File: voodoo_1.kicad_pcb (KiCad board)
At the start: 2 copper layers, 1 part, among them U1 LM301

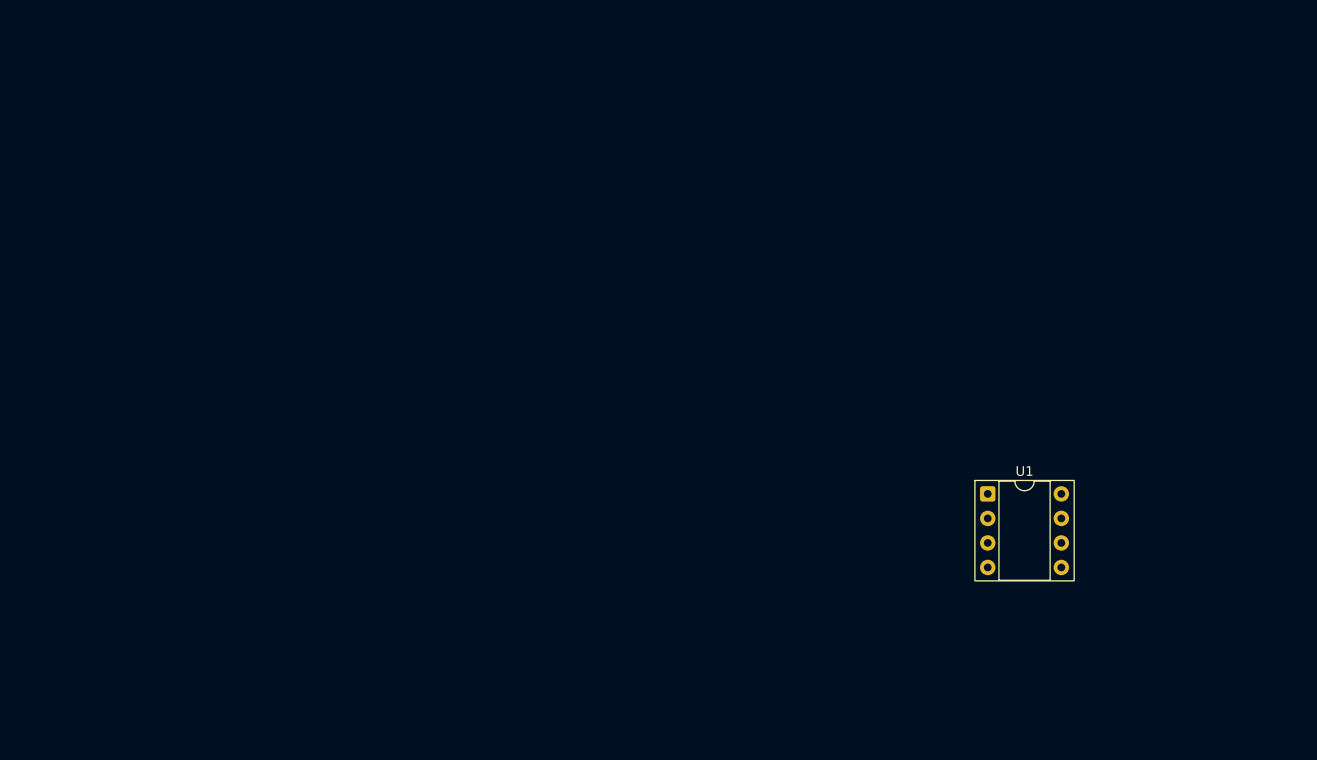
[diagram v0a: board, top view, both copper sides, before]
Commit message: フットプリント割り当て
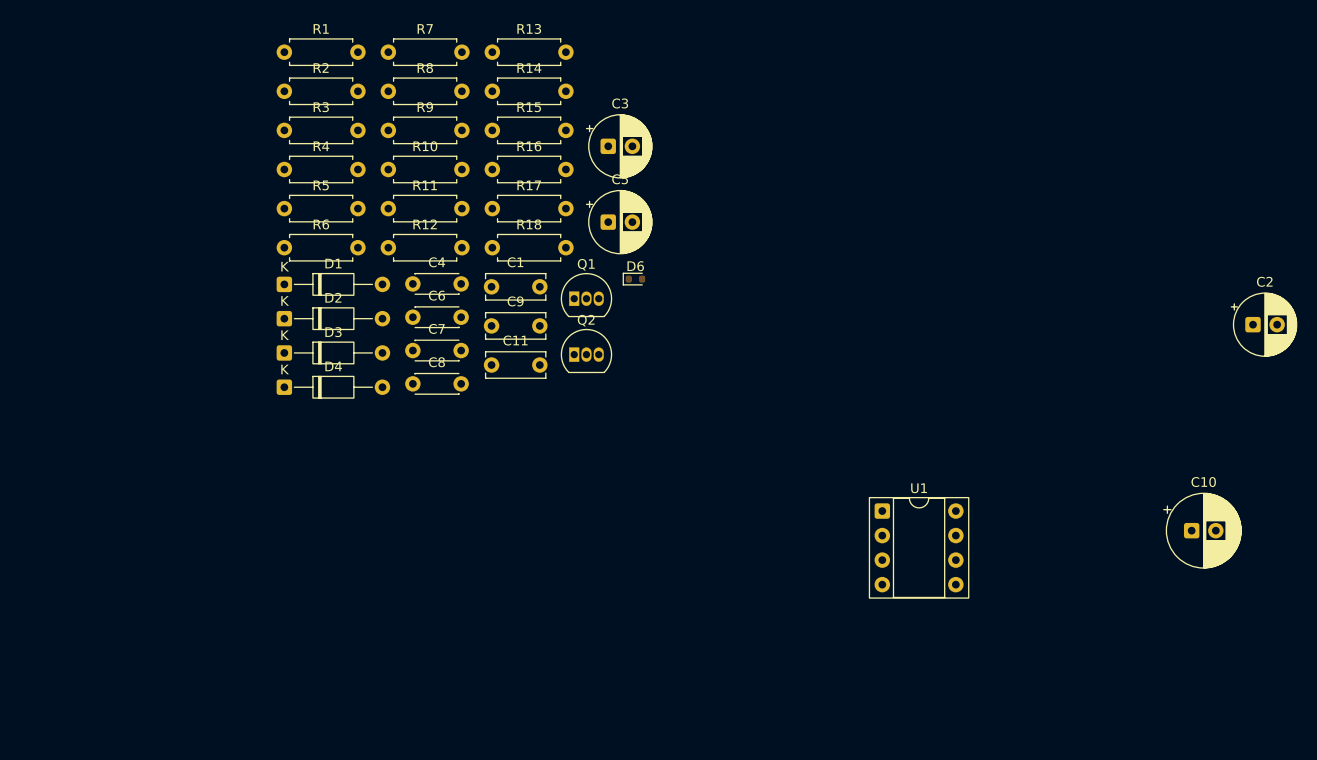
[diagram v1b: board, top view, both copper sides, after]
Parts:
- added C1: 0.1u, Capacitor_THT:C_Disc_D6.0mm_W2.5mm_P5.00mm, F.Cu at (88.8, 72.0)
- added C10: 16v220u, Capacitor_THT:CP_Radial_D7.5mm_P2.50mm, F.Cu at (161.3, 97.3)
- added C11: 0.1u, Capacitor_THT:C_Disc_D6.0mm_W2.5mm_P5.00mm, F.Cu at (88.8, 80.1)
- added C2: 16v22u, Capacitor_THT:CP_Radial_D6.3mm_P2.50mm, F.Cu at (167.7, 75.9)
- added C3: 16v2.2u, Capacitor_THT:CP_Radial_D6.3mm_P2.50mm, F.Cu at (100.9, 57.5)
- added C4: 22p, Capacitor_THT:C_Disc_D4.3mm_W1.9mm_P5.00mm, F.Cu at (80.7, 71.7)
- added C5: 16v2.2u, Capacitor_THT:CP_Radial_D6.3mm_P2.50mm, F.Cu at (100.9, 65.3)
- added C6: 3300p, Capacitor_THT:C_Disc_D4.3mm_W1.9mm_P5.00mm, F.Cu at (80.7, 75.2)
- added C7: 2200p, Capacitor_THT:C_Disc_D4.3mm_W1.9mm_P5.00mm, F.Cu at (80.7, 78.6)
- added C8: 470p, Capacitor_THT:C_Disc_D4.3mm_W1.9mm_P5.00mm, F.Cu at (80.7, 82.1)
- added C9: 0.1u, Capacitor_THT:C_Disc_D6.0mm_W2.5mm_P5.00mm, F.Cu at (88.8, 76.1)
- added D1: 1N4148WT, Diode_THT:D_DO-35_SOD27_P10.16mm_Horizontal, F.Cu at (67.4, 71.8)
- added D2: 1N4148WT, Diode_THT:D_DO-35_SOD27_P10.16mm_Horizontal, F.Cu at (67.4, 75.3)
- added D3: 1N4148WT, Diode_THT:D_DO-35_SOD27_P10.16mm_Horizontal, F.Cu at (67.4, 78.9)
- added D4: 1N4148WT, Diode_THT:D_DO-35_SOD27_P10.16mm_Horizontal, F.Cu at (67.4, 82.4)
- added D6: 1N4148WT, Diode_SMD:D_SOD-523, F.Cu at (103.7, 71.2)
- added Q1: 2N2222, Package_TO_SOT_THT:TO-92_Inline, F.Cu at (97.4, 73.3)
- added Q2: 2N2222, Package_TO_SOT_THT:TO-92_Inline, F.Cu at (97.4, 79.0)
- added R1: 2.2M, Resistor_THT:R_Axial_DIN0207_L6.3mm_D2.5mm_P7.62mm_Horizontal, F.Cu at (67.4, 47.7)
- added R10: 39k, Resistor_THT:R_Axial_DIN0207_L6.3mm_D2.5mm_P7.62mm_Horizontal, F.Cu at (78.1, 59.9)
- added R11: 39k, Resistor_THT:R_Axial_DIN0207_L6.3mm_D2.5mm_P7.62mm_Horizontal, F.Cu at (78.1, 63.9)
- added R12: 5.6k, Resistor_THT:R_Axial_DIN0207_L6.3mm_D2.5mm_P7.62mm_Horizontal, F.Cu at (78.1, 68.0)
- added R13: 12k, Resistor_THT:R_Axial_DIN0207_L6.3mm_D2.5mm_P7.62mm_Horizontal, F.Cu at (88.9, 47.7)
- added R14: 150, Resistor_THT:R_Axial_DIN0207_L6.3mm_D2.5mm_P7.62mm_Horizontal, F.Cu at (88.9, 51.8)
- added R15: 820k, Resistor_THT:R_Axial_DIN0207_L6.3mm_D2.5mm_P7.62mm_Horizontal, F.Cu at (88.9, 55.8)
- added R16: 1M, Resistor_THT:R_Axial_DIN0207_L6.3mm_D2.5mm_P7.62mm_Horizontal, F.Cu at (88.9, 59.9)
- added R17: 10k, Resistor_THT:R_Axial_DIN0207_L6.3mm_D2.5mm_P7.62mm_Horizontal, F.Cu at (88.9, 63.9)
- added R18: 2.2M, Resistor_THT:R_Axial_DIN0207_L6.3mm_D2.5mm_P7.62mm_Horizontal, F.Cu at (88.9, 68.0)
- added R2: 2.2M, Resistor_THT:R_Axial_DIN0207_L6.3mm_D2.5mm_P7.62mm_Horizontal, F.Cu at (67.4, 51.8)
- added R3: 680k, Resistor_THT:R_Axial_DIN0207_L6.3mm_D2.5mm_P7.62mm_Horizontal, F.Cu at (67.4, 55.8)
- added R4: 47k, Resistor_THT:R_Axial_DIN0207_L6.3mm_D2.5mm_P7.62mm_Horizontal, F.Cu at (67.4, 59.9)
- added R5: 47k, Resistor_THT:R_Axial_DIN0207_L6.3mm_D2.5mm_P7.62mm_Horizontal, F.Cu at (67.4, 63.9)
- added R6: 22k, Resistor_THT:R_Axial_DIN0207_L6.3mm_D2.5mm_P7.62mm_Horizontal, F.Cu at (67.4, 68.0)
- added R7: 150k, Resistor_THT:R_Axial_DIN0207_L6.3mm_D2.5mm_P7.62mm_Horizontal, F.Cu at (78.1, 47.7)
- added R8: 10k, Resistor_THT:R_Axial_DIN0207_L6.3mm_D2.5mm_P7.62mm_Horizontal, F.Cu at (78.1, 51.8)
- added R9: 1.5k, Resistor_THT:R_Axial_DIN0207_L6.3mm_D2.5mm_P7.62mm_Horizontal, F.Cu at (78.1, 55.8)
- U1: value LM301 -> LM308
- moved U1 11.1 mm to (129.3, 95.2)
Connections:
- U1 pad 1: unconnected-(U1-COMP1-Pad1) -> Net-(U1-COMP1)
- U1 pad 2: unconnected-(U1---Pad2) -> Net-(U1--)
- U1 pad 3: unconnected-(U1-+-Pad3) -> Net-(Q1-C)
- U1 pad 6: unconnected-(U1-Pad6) -> Net-(U1-COMP1)
- U1 pad 7: unconnected-(U1-V+-Pad7) -> Net-(D6-K)
- U1 pad 8: unconnected-(U1-COMP2-Pad8) -> Net-(U1-COMP2)

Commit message: 部品を配置
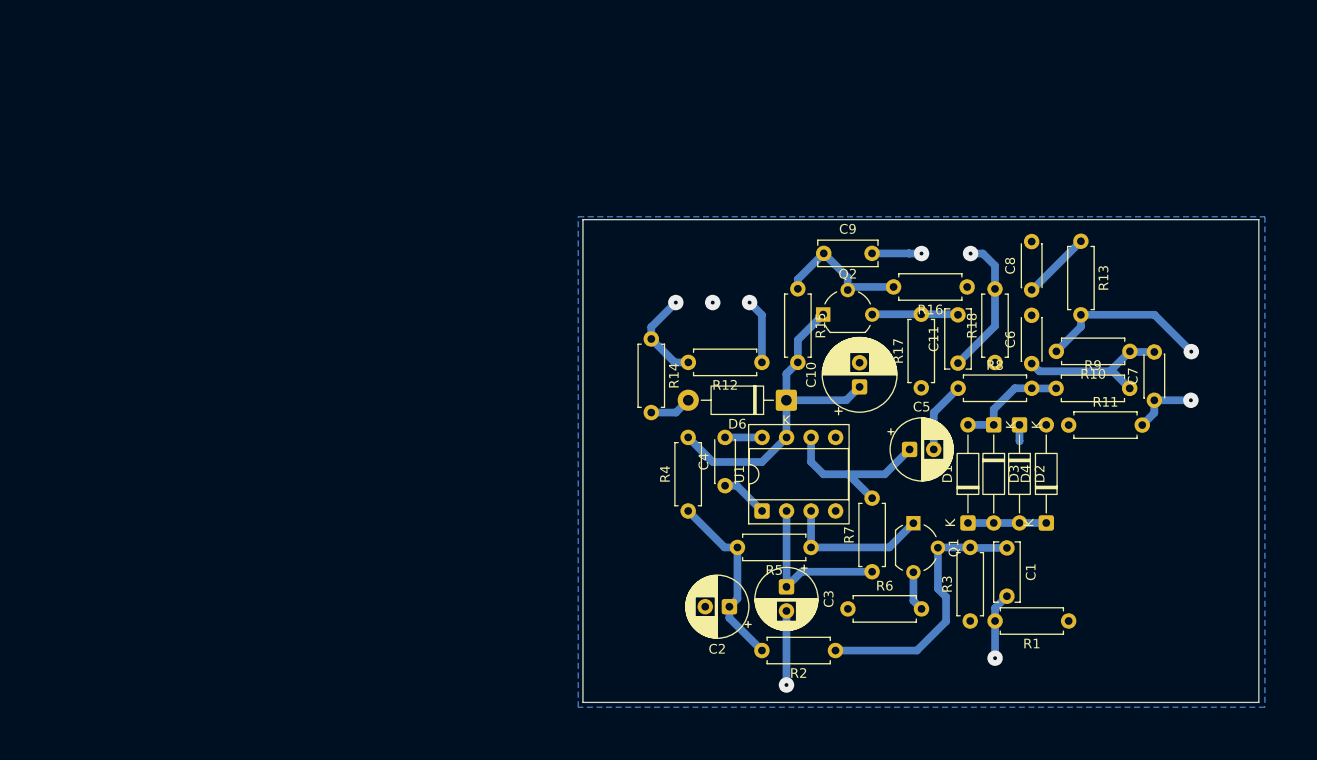
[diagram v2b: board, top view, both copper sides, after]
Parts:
- D6: value 1N4148WT -> 1N4001; footprint Diode_SMD:D_SOD-523 -> Diode_THT:D_DO-41_SOD81_P10.16mm_Horizontal
- Q1, Q2: footprint Package_TO_SOT_THT:TO-92_Inline -> Package_TO_SOT_THT:TO-92_Wide
- moved R1 100.3 mm to (148.6, 106.6), turned to 180 degrees
- moved R3 87.3 mm to (138.4, 106.6), turned to 90 degrees
- moved R2 81.3 mm to (124.4, 109.7), turned to 180 degrees
- moved D4 80.2 mm to (146.3, 96.5), turned to 90 degrees
- moved R10 79.1 mm to (154.9, 78.7), turned to 180 degrees
- moved C7 77.0 mm to (157.5, 83.8), turned to 90 degrees
- moved D2 76.9 mm to (143.5, 86.3), turned to -90 degrees
- moved D1 75.0 mm to (138.2, 96.5), turned to 90 degrees
- moved R9 74.1 mm to (147.3, 82.5)
- moved R11 73.9 mm to (148.6, 86.3)
- moved D3 73.8 mm to (140.8, 86.3), turned to -90 degrees
- moved R7 73.5 mm to (128.2, 101.5), turned to 90 degrees
- moved R6 69.3 mm to (125.7, 105.4)
- moved R8 66.6 mm to (137.1, 82.5)
- moved R5 64.9 mm to (121.9, 99.0), turned to 180 degrees
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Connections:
- C5 pad 1: Net-(U1-COMP1) -> Net-(C5-Pad1)
- R10 pad 2: Net-(C8-Pad1) -> Net-(R10-Pad2)
- R13 pad 2: Net-(C8-Pad1) -> Net-(R10-Pad2)
- R7 pad 2: Net-(U1-COMP1) -> Net-(C5-Pad1)
- U1 pad 6: Net-(U1-COMP1) -> Net-(C5-Pad1)
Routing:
- net Net-(D6-K): track 0.00 -> 34.8 mm
- net Net-(Q1-B): track 0.00 -> 27.9 mm
- net Net-(C2-Pad1): track 0.00 -> 19.1 mm
- net Net-(R10-Pad2): track 0.00 -> 17.8 mm, vias 0 -> 1
- net Net-(C5-Pad1): track 0.00 -> 17.8 mm
- net Net-(U1--): track 0.00 -> 17.4 mm
- net Net-(C6-Pad1): track 0.00 -> 16.7 mm
- net Net-(Q1-C): track 0.00 -> 15.5 mm
- net Net-(SW1B-C): track 0.00 -> 14.7 mm, vias 0 -> 1
- net Net-(Q2-B): track 0.00 -> 14.7 mm
- net Net-(D1-A): track 0.00 -> 11.7 mm
- net +9V: track 0.00 -> 9.67 mm, vias 0 -> 1
- net Net-(Q2-E): track 0.00 -> 8.95 mm
- net Net-(D1-K): track 0.00 -> 8.11 mm
- net Net-(C3-Pad2): track 0.00 -> 7.69 mm, vias 0 -> 1
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- added copper zone on B.Cu, net GND
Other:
- board outline added: 70 x 50 mm
